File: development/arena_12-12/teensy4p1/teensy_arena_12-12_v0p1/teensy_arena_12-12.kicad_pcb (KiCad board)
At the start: 6 copper layers, 228.6 x 228.6 mm, 445 parts, among them J1 Barrel_Jack, J2 Conn_01x04, J3 Conn_01x04, J4 Barrel_Jack, P1 CONN15, P10 CONN15, P11 CONN15, P12 CONN15, P2 CONN15, P3 CONN15, P4 CONN15, P5 CONN15, P6 CONN15, P7 CONN15, P8 CONN15, P9 CONN15, Q1 MOSFET_NCHAN, SW1 SW_SPDT, U1 Teensy4.1, U10 TXB0108PW, U11 TXB0108PW, U12 TXB0108PW, U13 TXB0108PW, U14 TXB0108PW, U15 74LVC1G17, U16 74LVC1G17, U17 74LVC1G17, U18 74LVC1G17, U19 74LVC2G17, U2 74LVC2G17, U20 74LVC2G17, U21 74LVC2G17, U22 74LVC2G17, U23 74LVC2G17, U24 74LVC2G17, U25 74LVC2G17, U26 74LVC2G17, U27 74LVC2G17, U28 74LVC2G17, U29 74LVC2G17, U3 TXB0108PW, U30 74LVC2G17, U31 74LVC2G17, U32 74LVC2G17, U33 74LVC2G17, U34 74LVC2G17, U35 74LVC2G17, U36 74LVC2G17, U37 74LVC2G17, U38 74LVC2G17, U39 74LVC2G17, U4 TXB0108PW, U40 74LVC2G17, U41 74LVC2G17, U42 74LVC2G17, U43 74LVC2G17, U44 74LVC2G17, U45 74LVC2G17, U46 74LVC2G17, U47 74LVC2G17, U48 74LVC2G17, U49 74LVC2G17, U5 TXB0108PW, U50 74LVC2G17, U51 74LVC2G17, U52 74LVC2G17, U53 74LVC2G17, U54 74LVC2G17, U55 74LVC2G17, U56 74LVC2G17, U57 74LVC2G17, U58 74LVC2G17, U59 74LVC2G17, U6 TXB0108PW, U60 74LVC2G17, U61 74LVC2G17, U62 74LVC2G17, U63 74LVC2G17, U64 74LVC2G17, U65 74LVC2G17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

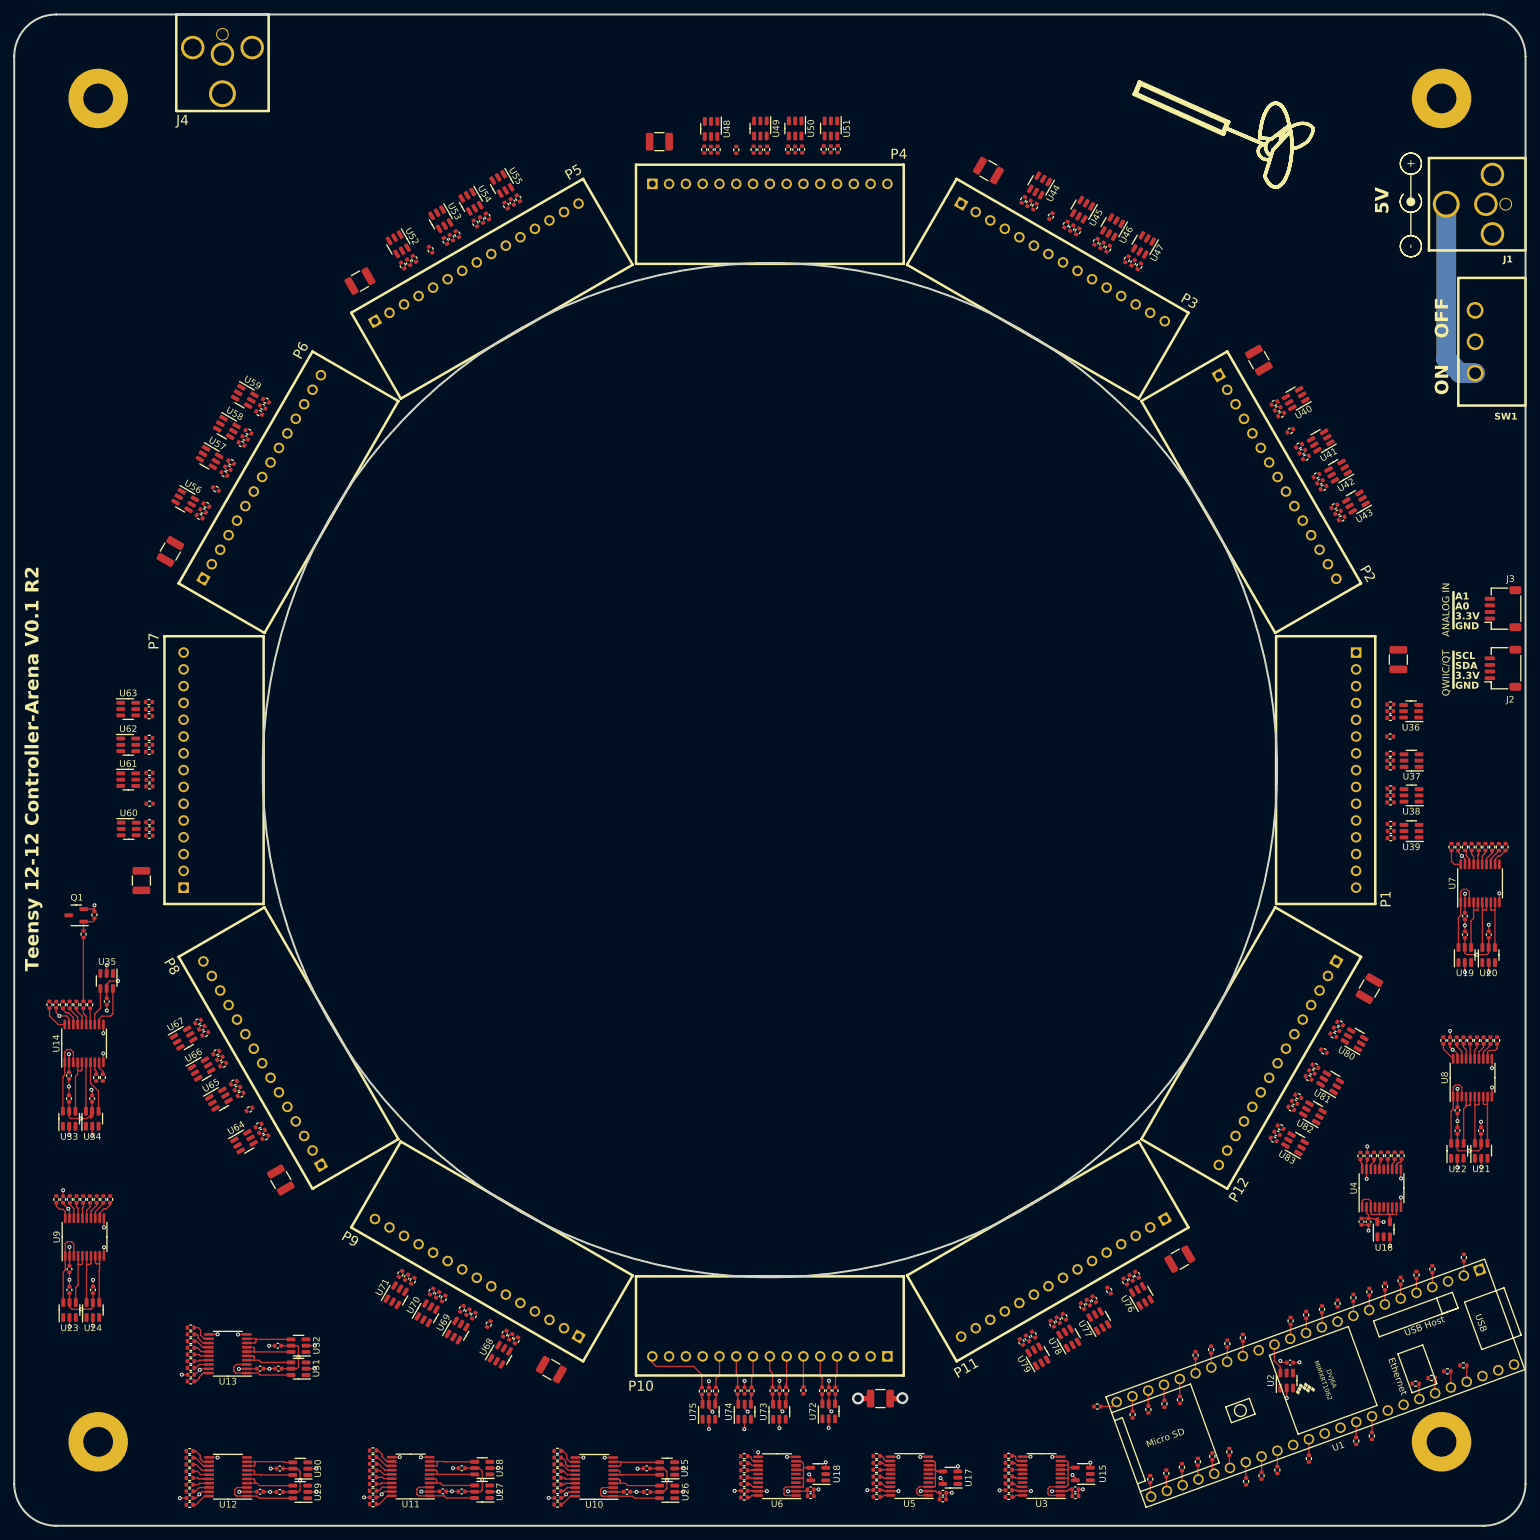
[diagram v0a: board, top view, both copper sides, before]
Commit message: Finished hand route of 12-12 teensy arena. Finished route of 12-12 top.
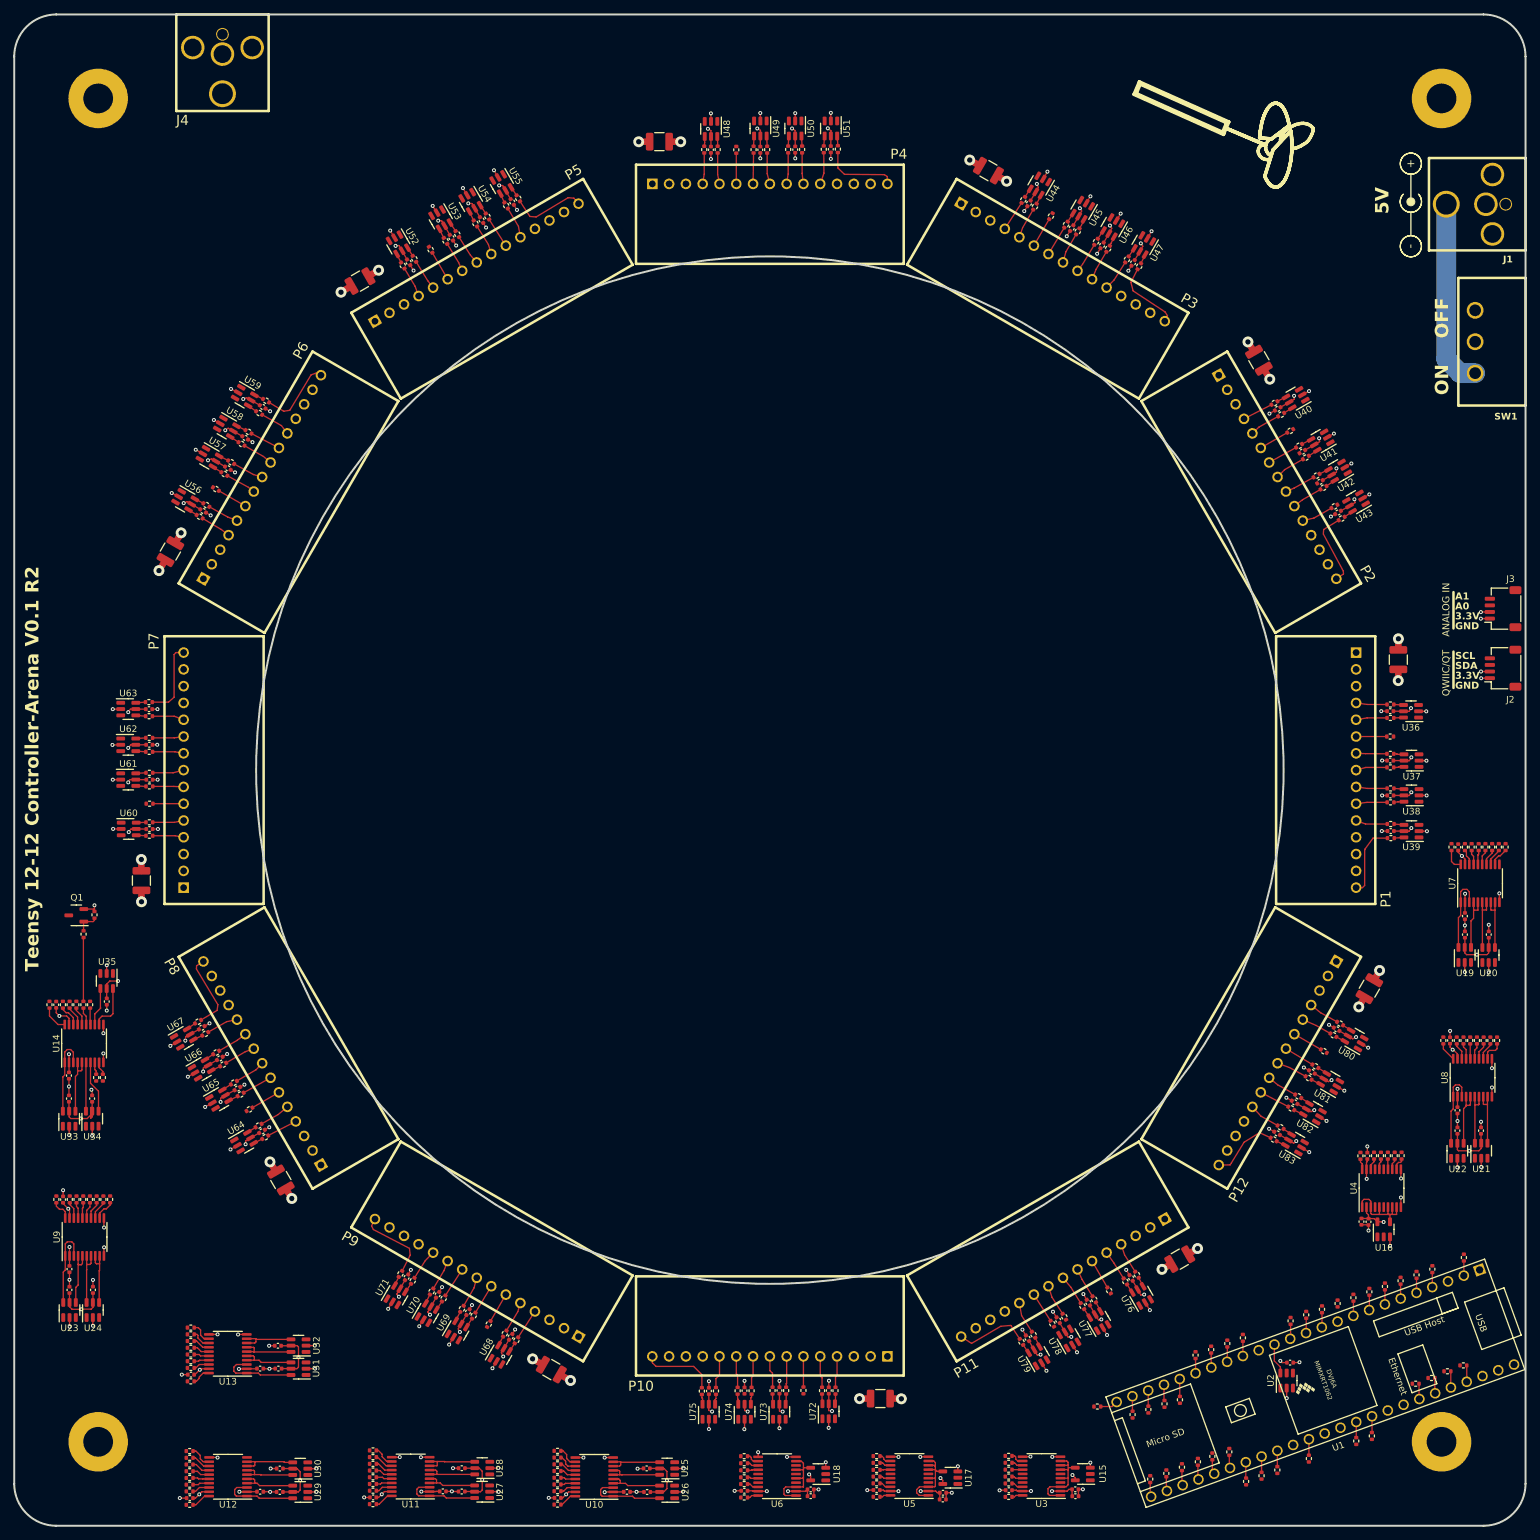
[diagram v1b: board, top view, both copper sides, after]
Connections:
- C47 pad 1: +3.3V -> +5V
- C48 pad 1: +3.3V -> +5V
- C49 pad 1: +3.3V -> +5V
- C50 pad 1: +3.3V -> +5V
- C51 pad 1: +3.3V -> +5V
- C52 pad 1: +3.3V -> +5V
- C53 pad 1: +3.3V -> +5V
- C54 pad 1: +3.3V -> +5V
- C55 pad 1: +3.3V -> +5V
- C56 pad 1: +3.3V -> +5V
- C57 pad 1: +3.3V -> +5V
- C58 pad 1: +3.3V -> +5V
- C59 pad 1: +3.3V -> +5V
- C60 pad 1: +3.3V -> +5V
- C61 pad 1: +3.3V -> +5V
- C62 pad 1: +3.3V -> +5V
- C63 pad 1: +3.3V -> +5V
- C64 pad 1: +3.3V -> +5V
- C65 pad 1: +3.3V -> +5V
- C66 pad 1: +3.3V -> +5V
- C67 pad 1: +3.3V -> +5V
- C68 pad 1: +3.3V -> +5V
- C69 pad 1: +3.3V -> +5V
- C70 pad 1: +3.3V -> +5V
- C71 pad 1: +3.3V -> +5V
- C72 pad 1: +3.3V -> +5V
- C73 pad 1: +3.3V -> +5V
- C74 pad 1: +3.3V -> +5V
- C75 pad 1: +3.3V -> +5V
- C76 pad 1: +3.3V -> +5V
- C77 pad 1: +3.3V -> +5V
- C78 pad 1: +3.3V -> +5V
- C79 pad 1: +3.3V -> +5V
- C80 pad 1: +3.3V -> +5V
- C81 pad 1: +3.3V -> +5V
- C82 pad 1: +3.3V -> +5V
- C83 pad 1: +3.3V -> +5V
- C84 pad 1: +3.3V -> +5V
- C85 pad 1: +3.3V -> +5V
- C86 pad 1: +3.3V -> +5V
- C87 pad 1: +3.3V -> +5V
- C88 pad 1: +3.3V -> +5V
- C89 pad 1: +3.3V -> +5V
- C90 pad 1: +3.3V -> +5V
- C91 pad 1: +3.3V -> +5V
- C92 pad 1: +3.3V -> +5V
- C93 pad 1: +3.3V -> +5V
- C94 pad 1: +3.3V -> +5V
- U36 pad 5: +3.3V -> +5V
- U37 pad 5: +3.3V -> +5V
- U38 pad 5: +3.3V -> +5V
- U39 pad 5: +3.3V -> +5V
- U40 pad 5: +3.3V -> +5V
- U41 pad 5: +3.3V -> +5V
- U42 pad 5: +3.3V -> +5V
- U43 pad 5: +3.3V -> +5V
- U44 pad 5: +3.3V -> +5V
- U45 pad 5: +3.3V -> +5V
- U46 pad 5: +3.3V -> +5V
- U47 pad 5: +3.3V -> +5V
- U48 pad 5: +3.3V -> +5V
- U49 pad 5: +3.3V -> +5V
- U50 pad 5: +3.3V -> +5V
- U51 pad 5: +3.3V -> +5V
- U52 pad 5: +3.3V -> +5V
- U53 pad 5: +3.3V -> +5V
- U54 pad 5: +3.3V -> +5V
- U55 pad 5: +3.3V -> +5V
- U56 pad 5: +3.3V -> +5V
- U57 pad 5: +3.3V -> +5V
- U58 pad 5: +3.3V -> +5V
- U59 pad 5: +3.3V -> +5V
- U60 pad 5: +3.3V -> +5V
- U61 pad 5: +3.3V -> +5V
- U62 pad 5: +3.3V -> +5V
- U63 pad 5: +3.3V -> +5V
- U64 pad 5: +3.3V -> +5V
- U65 pad 5: +3.3V -> +5V
- U66 pad 5: +3.3V -> +5V
- U67 pad 5: +3.3V -> +5V
- U68 pad 5: +3.3V -> +5V
- U69 pad 5: +3.3V -> +5V
- U70 pad 5: +3.3V -> +5V
- U71 pad 5: +3.3V -> +5V
- U72 pad 5: +3.3V -> +5V
- U73 pad 5: +3.3V -> +5V
- U74 pad 5: +3.3V -> +5V
- U75 pad 5: +3.3V -> +5V
- U76 pad 5: +3.3V -> +5V
- U77 pad 5: +3.3V -> +5V
- U78 pad 5: +3.3V -> +5V
- U79 pad 5: +3.3V -> +5V
- U80 pad 5: +3.3V -> +5V
- U81 pad 5: +3.3V -> +5V
- U82 pad 5: +3.3V -> +5V
- U83 pad 5: +3.3V -> +5V
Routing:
- net +5V: track 36.7 -> 196.7 mm, vias 13 -> 72
- net GND: track 98.7 -> 210.9 mm, vias 75 -> 174
- net /Panel Headers/HDR_EXT_INT_P8: track 0.00 -> 11.7 mm
- net /Panel Headers/HDR_EXT_INT_P9: track 0.00 -> 11.7 mm
- net /Panel Headers/HDR_EXT_INT_P7: track 0.00 -> 11.6 mm
- net /Panel Headers/HDR_EXT_INT_P2: track 0.00 -> 11.5 mm
- net /Panel Headers/HDR_EXT_INT_P4: track 0.00 -> 11.4 mm
- net /Panel Headers/HDR_EXT_INT_P6: track 0.00 -> 11.4 mm
- net /Panel Headers/HDR_EXT_INT_P5: track 0.00 -> 11.3 mm
- net /Panel Headers/HDR_EXT_INT_P1: track 0.00 -> 11.2 mm
- net /Panel Headers/HDR_EXT_INT_P11: track 0.00 -> 11.0 mm
- net /Panel Headers/HDR_EXT_INT_P3: track 0.00 -> 11.0 mm
- net /Panel Headers/HDR_EXT_INT_P12: track 0.00 -> 10.4 mm
- net +3.3V: track 142.4 -> 135.2 mm, vias 40 -> 38
- net /Panel Headers/HDR_CS_24_P11: track 0.00 -> 4.84 mm
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- added copper zone on In2.Cu, net +3.3V
- removed copper zone on In2.Cu, net +5V
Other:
- outline, holes or cut-outs redrawn
